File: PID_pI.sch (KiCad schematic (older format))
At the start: 31 parts

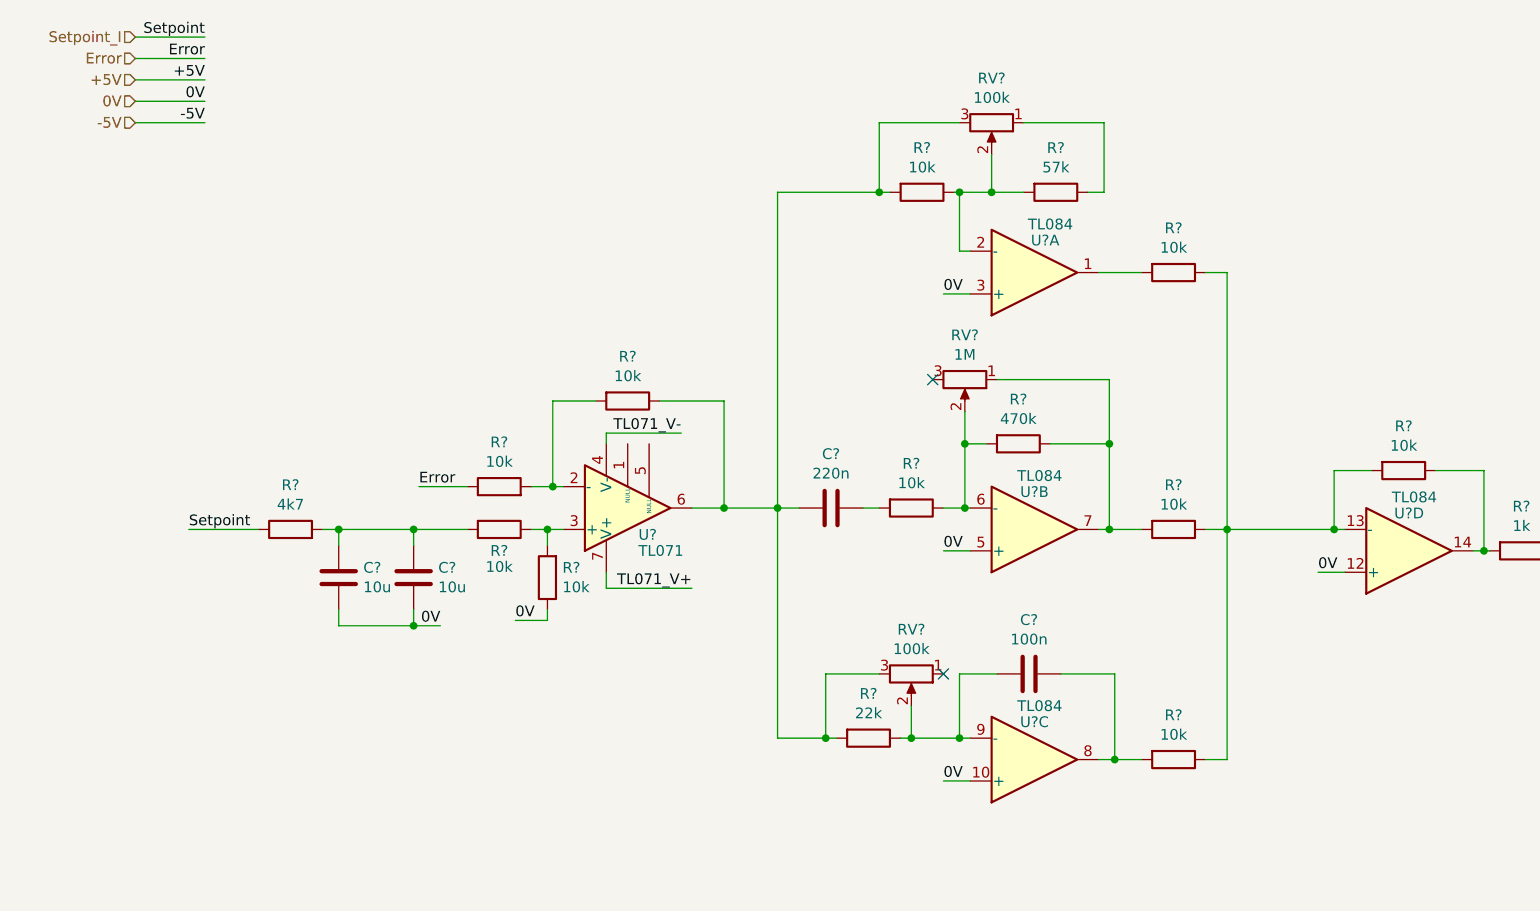
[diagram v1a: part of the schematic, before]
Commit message: Added jumpers to PID blocks
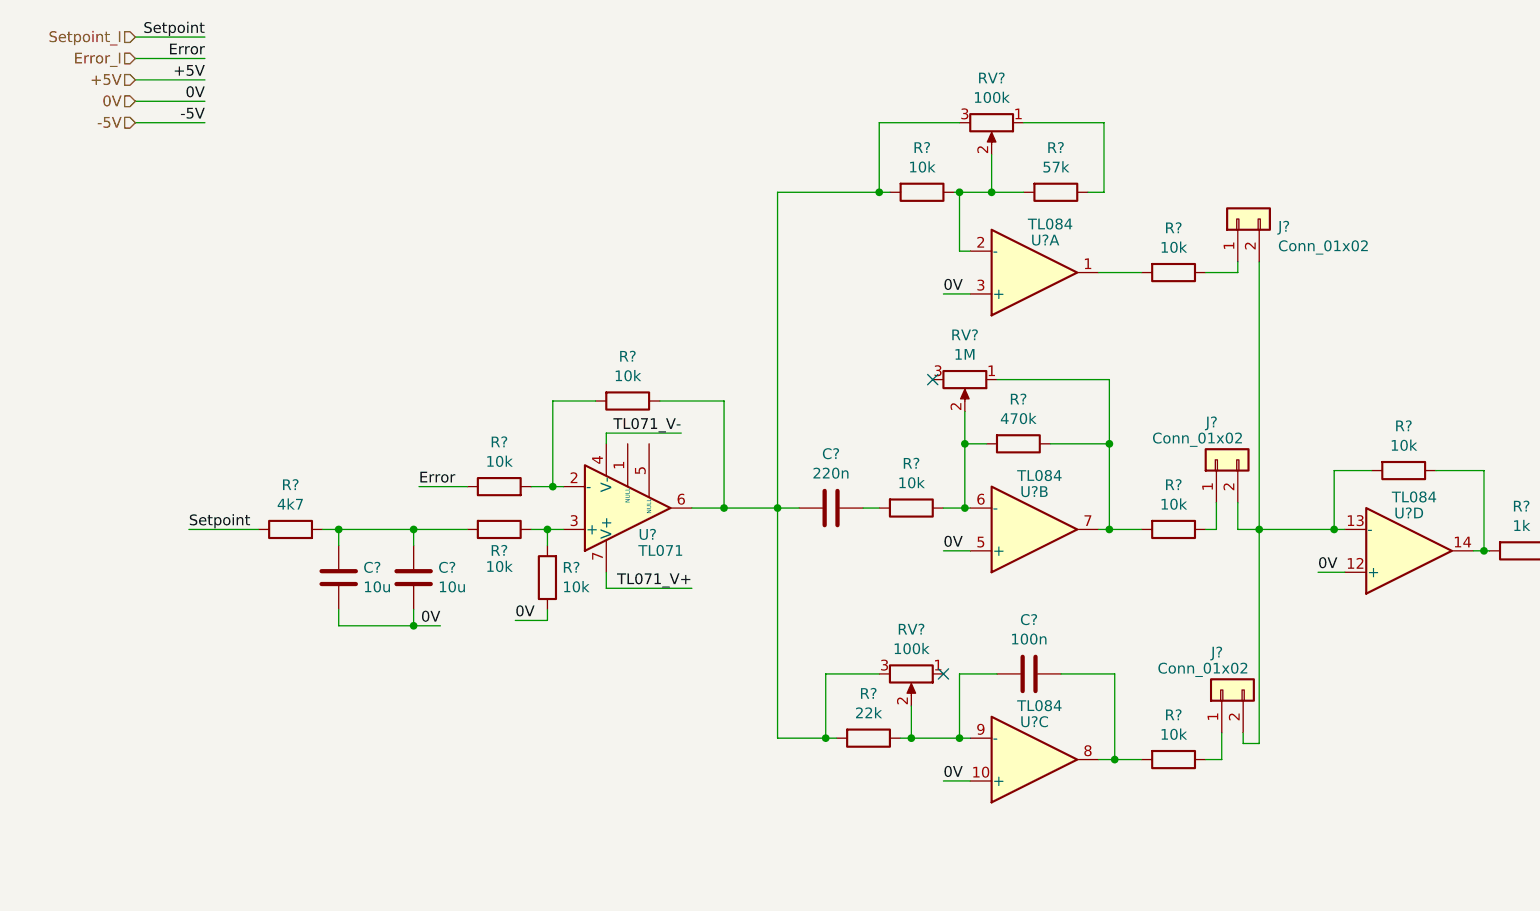
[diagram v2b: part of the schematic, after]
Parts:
- added J? (x3): Conn_01x02, symbol Connector_Generic:Conn_01x02
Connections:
- net Error renamed Error_I
- new net: J?.2 (Pin_2), J?.2 (Pin_2), J?.2 (Pin_2), R?.2, U?.13 (-)
- new net: J?.1 (Pin_1), R?.1 (x3)
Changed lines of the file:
@@
 $Descr A4 11693 8268
 encoding utf-8
-Sheet 13 12
+Sheet 12 12
 Title ""
 Date ""
@@
 AR Path="/61820F6B/6190CEB3" Ref="U?"  Part="1"
 AR Path="/61A28785/6190CEB3" Ref="U?"  Part="1"
+AR Path="/61A63B19/6190CEB3" Ref="U?"  Part="1"
 F 0 "U?" H 5200 1550 50  0000 C CNN
 F 1 "TL084" H 5225 1475 50  0000 C CNN
@@
 AR Path="/61820F6B/6190EA94" Ref="U?"  Part="2"
 AR Path="/61A28785/6190EA94" Ref="U?"  Part="2"
+AR Path="/61A63B19/6190EA94" Ref="U?"  Part="2"
 F 0 "U?" H 5150 2725 50  0000 C CNN
 F 1 "TL084" H 5175 2650 50  0000 C CNN
@@
 AR Path="/61820F6B/61910199" Ref="U?"  Part="3"
 AR Path="/61A28785/61910199" Ref="U?"  Part="3"
+AR Path="/61A63B19/61910199" Ref="U?"  Part="3"
 F 0 "U?" H 5150 3800 50  0000 C CNN
 F 1 "TL084" H 5175 3725 50  0000 C CNN
@@
 AR Path="/61820F6B/619111F1" Ref="U?"  Part="4"
 AR Path="/61A28785/619111F1" Ref="U?"  Part="4"
+AR Path="/61A63B19/619111F1" Ref="U?"  Part="4"
 F 0 "U?" H 6900 2825 50  0000 C CNN
 F 1 "TL084" H 6925 2750 50  0000 C CNN
@@
 AR Path="/61820F6B/619124C1" Ref="U?"  Part="5"
 AR Path="/61A28785/619124C1" Ref="U?"  Part="5"
+AR Path="/61A63B19/619124C1" Ref="U?"  Part="5"
 F 0 "U?" H 1808 6996 50  0000 L CNN
 F 1 "TL084" H 1808 6905 50  0000 L CNN
@@
 Setpoint_I
 Text HLabel 950  700  0    50   Input ~ 0
-Error
+Error_I
 Text HLabel 950  800  0    50   Input ~ 0
 +5V
@@
 AR Path="/61820F6B/619347E4" Ref="C?"  Part="1"
 AR Path="/61A28785/619347E4" Ref="C?"  Part="1"
+AR Path="/61A63B19/619347E4" Ref="C?"  Part="1"
 F 0 "C?" H 1465 6796 50  0000 L CNN
 F 1 "100n" H 1465 6705 50  0000 L CNN
@@
 AR Path="/61820F6B/6193524E" Ref="C?"  Part="1"
 AR Path="/61A28785/6193524E" Ref="C?"  Part="1"
+AR Path="/61A63B19/6193524E" Ref="C?"  Part="1"
 F 0 "C?" H 1465 7196 50  0000 L CNN
 F 1 "100n" H 1465 7105 50  0000 L CNN
@@
 AR Path="/61820F6B/61935E4A" Ref="R?"  Part="1"
 AR Path="/61A28785/61935E4A" Ref="R?"  Part="1"
+AR Path="/61A63B19/61935E4A" Ref="R?"  Part="1"
 F 0 "R?" V 4418 1325 50  0000 C CNN
 F 1 "10k" V 4509 1325 50  0000 C CNN
@@
 AR Path="/61820F6B/619366A7" Ref="R?"  Part="1"
 AR Path="/61A28785/619366A7" Ref="R?"  Part="1"
+AR Path="/61A63B19/619366A7" Ref="R?"  Part="1"
 F 0 "R?" V 5043 1325 50  0000 C CNN
 F 1 "57k" V 5134 1325 50  0000 C CNN
@@
 AR Path="/61820F6B/619368E6" Ref="R?"  Part="1"
 AR Path="/61A28785/619368E6" Ref="R?"  Part="1"
+AR Path="/61A63B19/619368E6" Ref="R?"  Part="1"
 F 0 "R?" V 5593 1700 50  0000 C CNN
 F 1 "10k" V 5684 1700 50  0000 C CNN
@@
 AR Path="/61820F6B/61936FF4" Ref="RV?"  Part="1"
 AR Path="/61A28785/61936FF4" Ref="RV?"  Part="1"
+AR Path="/61A63B19/61936FF4" Ref="RV?"  Part="1"
 F 0 "RV?" V 4743 1000 50  0000 C CNN
 F 1 "100k" V 4834 1000 50  0000 C CNN
@@
 AR Path="/61820F6B/61943F9E" Ref="RV?"  Part="1"
 AR Path="/61A28785/61943F9E" Ref="RV?"  Part="1"
+AR Path="/61A63B19/61943F9E" Ref="RV?"  Part="1"
 F 0 "RV?" V 4618 2200 50  0000 C CNN
 F 1 "1M" V 4709 2200 50  0000 C CNN
@@
 AR Path="/61820F6B/61944E14" Ref="R?"  Part="1"
 AR Path="/61A28785/61944E14" Ref="R?"  Part="1"
+AR Path="/61A63B19/61944E14" Ref="R?"  Part="1"
 F 0 "R?" V 4868 2500 50  0000 C CNN
 F 1 "470k" V 4959 2500 50  0000 C CNN
@@
 AR Path="/61820F6B/6194AB1B" Ref="R?"  Part="1"
 AR Path="/61A28785/6194AB1B" Ref="R?"  Part="1"
+AR Path="/61A63B19/6194AB1B" Ref="R?"  Part="1"
 F 0 "R?" V 5593 2900 50  0000 C CNN
 F 1 "10k" V 5684 2900 50  0000 C CNN
@@
 AR Path="/61820F6B/6194CA5C" Ref="R?"  Part="1"
 AR Path="/61A28785/6194CA5C" Ref="R?"  Part="1"
+AR Path="/61A63B19/6194CA5C" Ref="R?"  Part="1"
 F 0 "R?" V 4368 2800 50  0000 C CNN
 F 1 "10k" V 4459 2800 50  0000 C CNN
@@
 AR Path="/61820F6B/6194E347" Ref="C?"  Part="1"
 AR Path="/61A28785/6194E347" Ref="C?"  Part="1"
+AR Path="/61A63B19/6194E347" Ref="C?"  Part="1"
 F 0 "C?" V 3948 2800 50  0000 C CNN
 F 1 "220n" V 4039 2800 50  0000 C CNN
@@
 AR Path="/61820F6B/61951D7A" Ref="RV?"  Part="1"
 AR Path="/61A28785/61951D7A" Ref="RV?"  Part="1"
+AR Path="/61A63B19/61951D7A" Ref="RV?"  Part="1"
 F 0 "RV?" V 4368 3575 50  0000 C CNN
 F 1 "100k" V 4459 3575 50  0000 C CNN
@@
 AR Path="/61820F6B/61956CC5" Ref="R?"  Part="1"
 AR Path="/61A28785/61956CC5" Ref="R?"  Part="1"
+AR Path="/61A63B19/61956CC5" Ref="R?"  Part="1"
 F 0 "R?" V 4168 3875 50  0000 C CNN
 F 1 "22k" V 4259 3875 50  0000 C CNN
@@
 AR Path="/61820F6B/6195B27F" Ref="C?"  Part="1"
 AR Path="/61A28785/6195B27F" Ref="C?"  Part="1"
+AR Path="/61A63B19/6195B27F" Ref="C?"  Part="1"
 F 0 "C?" V 4873 3575 50  0000 C CNN
 F 1 "100n" V 4964 3575 50  0000 C CNN
@@
 AR Path="/61820F6B/619625D8" Ref="R?"  Part="1"
 AR Path="/61A28785/619625D8" Ref="R?"  Part="1"
+AR Path="/61A63B19/619625D8" Ref="R?"  Part="1"
 F 0 "R?" V 5593 3975 50  0000 C CNN
 F 1 "10k" V 5684 3975 50  0000 C CNN
@@
 	5650 3975 5525 3975
 Connection ~ 5525 3975
-Wire Wire Line
-	5950 1700 6050 1700
-Wire Wire Line
-	6050 1700 6050 2900
-Wire Wire Line
-	6050 2900 5950 2900
-Wire Wire Line
-	6050 2900 6050 3975
-Wire Wire Line
-	6050 3975 5950 3975
-Connection ~ 6050 2900
 Wire Wire Line
 	1350 7000 1350 6950
@@
 AR Path="/61820F6B/61982F00" Ref="R?"  Part="1"
 AR Path="/61A28785/61982F00" Ref="R?"  Part="1"
+AR Path="/61A63B19/61982F00" Ref="R?"  Part="1"
 F 0 "R?" V 6668 2625 50  0000 C CNN
 F 1 "10k" V 6759 2625 50  0000 C CNN
@@
 Wire Wire Line
 	6550 2900 6600 2900
-Wire Wire Line
-	6050 2900 6550 2900
-Connection ~ 6550 2900
 Text Label 6475 3100 0    50   ~ 0
 0V
@@
 AR Path="/61820F6B/619938D0" Ref="R?"  Part="1"
 AR Path="/61A28785/619938D0" Ref="R?"  Part="1"
+AR Path="/61A63B19/619938D0" Ref="R?"  Part="1"
 F 0 "R?" V 7218 3000 50  0000 C CNN
 F 1 "1k" V 7309 3000 50  0000 C CNN
@@
 AR Path="/61820F6B/619A4A1D" Ref="R?"  Part="1"
 AR Path="/61A28785/619A4A1D" Ref="R?"  Part="1"
+AR Path="/61A63B19/619A4A1D" Ref="R?"  Part="1"
 F 0 "R?" V 3043 2300 50  0000 C CNN
 F 1 "10k" V 3134 2300 50  0000 C CNN
@@
 AR Path="/61820F6B/6199C115" Ref="U?"  Part="1"
 AR Path="/61A28785/6199C115" Ref="U?"  Part="1"
+AR Path="/61A63B19/6199C115" Ref="U?"  Part="1"
 F 0 "U?" H 3300 2925 50  0000 L CNN
 F 1 "TL071" H 3300 3000 50  0000 L CNN
@@
 AR Path="/61820F6B/619AE2CE" Ref="C?"  Part="1"
 AR Path="/61A28785/619AE2CE" Ref="C?"  Part="1"
+AR Path="/61A63B19/619AE2CE" Ref="C?"  Part="1"
 F 0 "C?" H 2590 6996 50  0000 L CNN
 F 1 "100n" H 2590 6905 50  0000 L CNN
@@
 AR Path="/61820F6B/619D83AD" Ref="R?"  Part="1"
 AR Path="/61A28785/619D83AD" Ref="R?"  Part="1"
+AR Path="/61A63B19/619D83AD" Ref="R?"  Part="1"
 F 0 "R?" V 2750 2900 50  0000 C CNN
 F 1 "10k" V 2825 2900 50  0000 C CNN
@@
 AR Path="/61820F6B/619D9316" Ref="R?"  Part="1"
 AR Path="/61A28785/619D9316" Ref="R?"  Part="1"
+AR Path="/61A63B19/619D9316" Ref="R?"  Part="1"
 F 0 "R?" H 2805 3079 50  0000 R CNN
 F 1 "10k" H 2805 3170 50  0000 R CNN
@@
 AR Path="/61820F6B/619E4FE6" Ref="R?"  Part="1"
 AR Path="/61A28785/619E4FE6" Ref="R?"  Part="1"
+AR Path="/61A63B19/619E4FE6" Ref="R?"  Part="1"
 F 0 "R?" V 2857 2700 50  0000 C CNN
 F 1 "10k" V 2766 2700 50  0000 C CNN
@@
 AR Path="/61820F6B/61A012A2" Ref="C?"  Part="1"
 AR Path="/61A28785/61A012A2" Ref="C?"  Part="1"
+AR Path="/61A63B19/61A012A2" Ref="C?"  Part="1"
 F 0 "C?" H 2135 3079 50  0000 R CNN
 F 1 "10u" H 2135 3170 50  0000 R CNN
@@
 AR Path="/61820F6B/61A023B8" Ref="C?"  Part="1"
 AR Path="/61A28785/61A023B8" Ref="C?"  Part="1"
+AR Path="/61A63B19/61A023B8" Ref="C?"  Part="1"
 F 0 "C?" H 1785 3079 50  0000 R CNN
 F 1 "10u" H 1785 3170 50  0000 R CNN
@@
 AR Path="/61820F6B/61A1C984" Ref="R?"  Part="1"
 AR Path="/61A28785/61A1C984" Ref="R?"  Part="1"
+AR Path="/61A63B19/61A1C984" Ref="R?"  Part="1"
 F 0 "R?" V 1882 2900 50  0000 C CNN
 F 1 "4k7" V 1791 2900 50  0000 C CNN
@@
 Wire Wire Line
 	1200 2900 1525 2900
+$Comp
+L Connector_Generic:Conn_01x02 J?
+U 1 1 61A3BD55
+P 6100 1450
+AR Path="/619B51F3/61A3BD55" Ref="J?"  Part="1"
+AR Path="/61A63B19/61A3BD55" Ref="J?"  Part="1"
+F 0 "J?" V 6064 1262 50  0000 R CNN
+F 1 "Conn_01x02" V 5973 1262 50  0000 R CNN
+F 2 "" H 6100 1450 50  0001 C CNN
+F 3 "~" H 6100 1450 50  0001 C CNN
+	1    6100 1450
+	0    -1   -1   0
+$EndComp
+Wire Wire Line
+	6100 1700 6100 1650
+Wire Wire Line
+	5950 1700 6100 1700
+$Comp
+L Connector_Generic:Conn_01x02 J?
+U 1 1 61A427D5
+P 6000 2575
+AR Path="/619B51F3/61A427D5" Ref="J?"  Part="1"
+AR Path="/61A63B19/61A427D5" Ref="J?"  Part="1"
+F 0 "J?" V 6175 2625 50  0000 R CNN
+F 1 "Conn_01x02" V 6100 2875 50  0000 R CNN
+F 2 "" H 6000 2575 50  0001 C CNN
+F 3 "~" H 6000 2575 50  0001 C CNN
+	1    6000 2575
+	0    -1   -1   0
+$EndComp
+Wire Wire Line
+	5950 2900 6000 2900
+Wire Wire Line
+	6000 2900 6000 2775
+Wire Wire Line
+	6100 2775 6100 2900
+Wire Wire Line
+	6100 2900 6200 2900
+Connection ~ 6550 2900
+Wire Wire Line
+	6200 1650 6200 2900
+Connection ~ 6200 2900
+Wire Wire Line
+	6200 2900 6550 2900
+$Comp
+L Connector_Generic:Conn_01x02 J?
+U 1 1 61A533BF
+P 6025 3650
+AR Path="/619B51F3/61A533BF" Ref="J?"  Part="1"
+AR Path="/61A63B19/61A533BF" Ref="J?"  Part="1"
+F 0 "J?" V 6200 3700 50  0000 R CNN
+F 1 "Conn_01x02" V 6125 3950 50  0000 R CNN
+F 2 "" H 6025 3650 50  0001 C CNN
+F 3 "~" H 6025 3650 50  0001 C CNN
+	1    6025 3650
+	0    -1   -1   0
+$EndComp
+Wire Wire Line
+	6200 2900 6200 3900
+Wire Wire Line
+	5950 3975 6025 3975
+Wire Wire Line
+	6025 3850 6025 3975
+Wire Wire Line
+	6125 3850 6125 3900
+Wire Wire Line
+	6125 3900 6200 3900
 $EndSCHEMATC
